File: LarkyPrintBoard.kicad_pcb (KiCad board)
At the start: 2 copper layers, 35.1 x 51.6 mm, 18 parts, among them J1 EXT1_IN, J2 EXT2_IN, J3 EXT1_OUT, J4 EXT2_OUT, J5 UART, J6 EN, J7 BOOT, U1 LM1117-3.3, U2 ESP32-WROOM, U3 CBT3257A, U4 CBT3257A

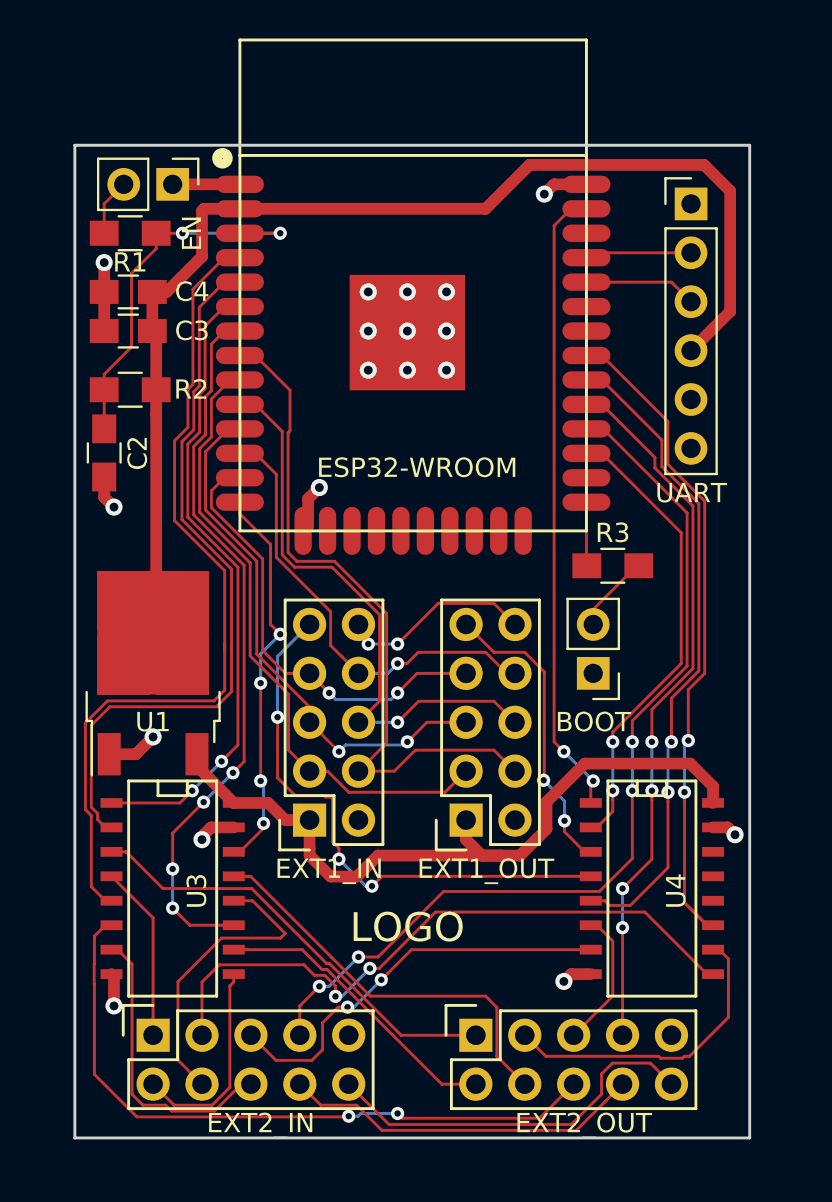
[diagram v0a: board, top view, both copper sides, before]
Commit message: Fix output pins on input only ESP32 pins. Add JTAG. Tweaks and improvements.
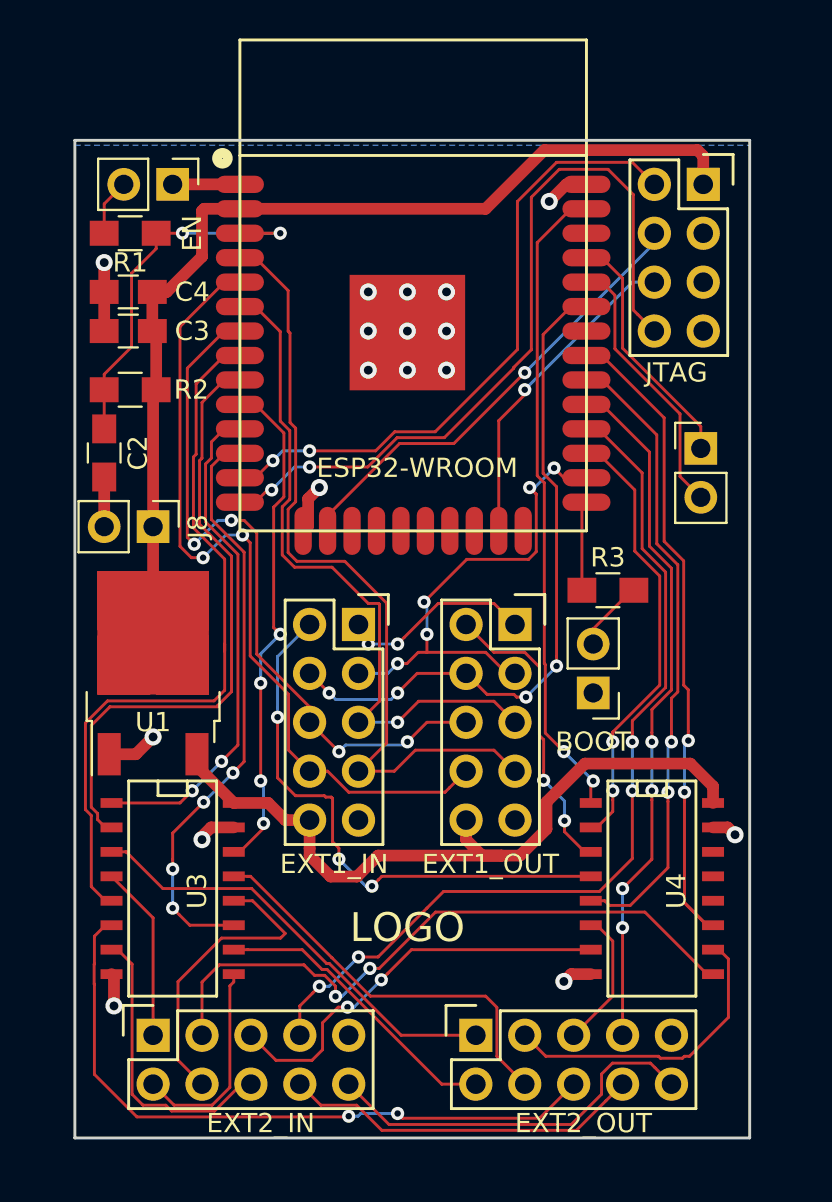
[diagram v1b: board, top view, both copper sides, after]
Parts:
- added J8: 3V3, Pin_Headers:Pin_Header_Straight_1x02_Pitch2.54mm, F.Cu at (149.4, 99.1)
- added J9: JTAG, Socket_Strips:Socket_Strip_Straight_2x04, F.Cu at (177.9, 81.3)
- J5: footprint Pin_Headers:Pin_Header_Straight_1x06_Pitch2.54mm -> Pin_Headers:Pin_Header_Straight_1x02_Pitch2.54mm
- moved J5 12.7 mm to (177.8, 95.0)
- moved J1 10.5 mm to (160.0, 104.1), turned to 270 degrees
- moved J3 10.5 mm to (168.1, 104.1), turned to 270 degrees
- moved R3 1.30 mm to (173.0, 102.4)
- moved J7 1.02 mm to (172.2, 107.7)
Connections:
- J1 pad 1: +5V -> /BEEP
- J1 pad 10: /BEEP -> +5V
- J1 pad 2: GND -> /ENC_BTN_I
- J1 pad 3: /LCD7 -> /LCD_EN
- J1 pad 4: /LCD6 -> /LCD_RS
- J1 pad 5: /LCD5 -> /LCD4
- J1 pad 6: /LCD4 -> /LCD5
- J1 pad 7: /LCD_RS -> /LCD6
- J1 pad 8: /LCD_EN -> /LCD7
- J1 pad 9: /ENC_BTN_I -> GND
- J3 pad 1: +5V -> /BEEP
- J3 pad 10: /BEEP -> +5V
- J3 pad 2: GND -> /ENC_BTN_O
- J3 pad 3: /LCD7 -> /LCD_EN
- J3 pad 4: /LCD6 -> /LCD_RS
- J3 pad 5: /LCD5 -> /LCD4
- J3 pad 6: /LCD4 -> /LCD5
- J3 pad 7: /LCD_RS -> /LCD6
- J3 pad 8: /LCD_EN -> /LCD7
- J3 pad 9: /ENC_BTN_O -> GND
- J5 pad 1: /DTR -> /ESP_TX
- J5 pad 2: /ESP_TX -> /ESP_RX
- U2 pad 10: /LCD4 -> /ESP_SD_SS
- U2 pad 11: /LCD5 -> /SD_MUX_S
- U2 pad 12: /LCD_EN -> /ESP_SPI_SCK
- U2 pad 13: /LCD_RS -> /JTAG_TMS
- U2 pad 14: /ESP_SD_SS -> /JTAG_TDI
- U2 pad 16: Net-(U2-Pad16) -> /JTAG_TCK
- U2 pad 23: Net-(U2-Pad23) -> /JTAG_TDO
- U2 pad 26: Net-(U2-Pad26) -> /LCD_EN
- U2 pad 33: Net-(U2-Pad33) -> /LCD_RS
- U2 pad 4: /ESP_SPI_MOSI -> /LCD6
- U2 pad 5: /ESP_SPI_MISO -> /LCD7
- U2 pad 6: /SD_MUX_S -> /LCD4
- U2 pad 7: /ESP_SPI_SCK -> /LCD5
- U2 pad 8: /LCD6 -> /ESP_SPI_MOSI
- U2 pad 9: /LCD7 -> /ESP_SPI_MISO
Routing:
- net /JTAG_TDI: track 0.00 -> 40.3 mm, vias 0 -> 2
- net /JTAG_TMS: track 0.00 -> 33.3 mm, vias 0 -> 2
- net /JTAG_TCK: track 0.00 -> 24.3 mm, vias 0 -> 1
- net /JTAG_TDO: track 0.00 -> 17.3 mm, vias 0 -> 1
- net /LCD_RS: track 23.3 -> 34.7 mm, vias 2 -> 4
- net /LCD5: track 28.0 -> 37.7 mm, vias 2 -> 4
- net /LCD7: track 32.9 -> 42.2 mm, vias 0 -> 2
- net +3V3: track 61.5 -> 52.6 mm
- net /ESP_RX: track 5.85 -> 14.1 mm
- net /ESP_TX: track 5.54 -> 13.2 mm
- net /ESP_SPI_SCK: track 37.6 -> 30.5 mm
- net /LCD4: track 30.6 -> 37.1 mm
- net /SD_MUX_S: track 33.3 -> 26.7 mm
- net /LCD6: track 36.1 -> 42.5 mm
- net /ESP_SD_SS: track 20.3 -> 26.3 mm
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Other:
- board size 35.1 x 51.6 mm -> 35.1 x 51.8 mm

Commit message: Alpha 1 final.
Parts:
- added D1: LED, LEDs:LED_0805_HandSoldering, F.Cu at (178.6, 107.4)
- added G***: LOGO, LarkyPrint:LOGO_17x8, F.Cu at (162.8, 120.7)
- added R4: 560, Resistors_SMD:R_0805_HandSoldering, F.Cu at (178.6, 102.1)
- added REF**: MountingHole_3mm, Mounting_Holes:MountingHole_3mm, F.Cu at (146.0, 78.0)
- added REF**: MountingHole_3mm, Mounting_Holes:MountingHole_3mm, F.Cu at (180.0, 78.0)
- added REF**: MountingHole_3mm, Mounting_Holes:MountingHole_3mm, F.Cu at (180.0, 130.0)
- added REF**: MountingHole_3mm, Mounting_Holes:MountingHole_3mm, F.Cu at (146.0, 130.0)
- J6: value EN -> RST
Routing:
- net +3V3: track 52.6 -> 73.4 mm
- net Net-(D1-Pad2): track 0.00 -> 2.63 mm
- net GND: track 23.8 -> 25.8 mm, vias 17 -> 18
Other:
- board size 35.1 x 51.8 mm -> 38 x 56 mm
- board text added: "Lark R1-A1 - 09.07.2017 Copyright Greg Lincoln CC BY-NC-SA"
- board text removed: "LOGO"
- board text removed: "LarkyPrint v0r1 - MM/DD/YYYY Some rights reserved."

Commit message: Tons of changes and fixes. R1A2
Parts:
- removed J9: JTAG, Socket_Strips:Socket_Strip_Straight_2x04
- removed the REF** at (146.0, 78.0)
- removed the REF** at (180.0, 78.0)
- removed the REF** at (180.0, 130.0)
- removed the REF** at (146.0, 130.0)
- removed the REF*** at (163.1, 96.5)
- added G***: LOGO, LarkyPrint:LOGO, B.Cu at (162.6, 80.8)
- added R10: 10K, Resistors_SMD:R_0805_HandSoldering, F.Cu at (148.8, 101.9)
- added R11: 680, Resistors_SMD:R_0805_HandSoldering, F.Cu at (173.0, 104.1)
- added R5: 10K, Resistors_SMD:R_0805_HandSoldering, F.Cu at (157.2, 119.7)
- added R6: 10K, Resistors_SMD:R_0805_HandSoldering, F.Cu at (168.7, 119.7)
- added R7: 10K, Resistors_SMD:R_0805_HandSoldering, F.Cu at (178.6, 112.5)
- added R8: 10K, Resistors_SMD:R_0805_HandSoldering, F.Cu at (147.3, 113.7)
- added R9: 10K, Resistors_SMD:R_0805_HandSoldering, F.Cu at (148.8, 103.6)
- added REF**: MountingHole_2.2mm_M2, Mounting_Holes:MountingHole_2.2mm_M2, F.Cu at (146.0, 130.0)
- added REF**: MountingHole_2.2mm_M2, Mounting_Holes:MountingHole_2.2mm_M2, F.Cu at (180.0, 130.0)
- added REF**: MountingHole_2.2mm_M2, Mounting_Holes:MountingHole_2.2mm_M2, F.Cu at (180.0, 78.0)
- added REF***: OSHW-Logo_5.7x6mm_SilkScreen, Symbols:OSHW-Logo_5.7x6mm_SilkScreen, B.Cu at (162.8, 97.2)
- C3: footprint Capacitors_SMD:C_0805_HandSoldering -> Capacitors_SMD:C_1206_HandSoldering
- J1: value EXT1_IN -> EXT1 Printer; footprint Socket_Strips:Socket_Strip_Straight_2x05 -> Pin_Headers:Pin_Header_Straight_2x05_Pitch2.54mm
- J2: value EXT2_IN -> EXT2 LCD; footprint Socket_Strips:Socket_Strip_Straight_2x05 -> Pin_Headers:Pin_Header_Straight_2x05_Pitch2.54mm
- J3: value EXT1_OUT -> EXT1 LCD; footprint Socket_Strips:Socket_Strip_Straight_2x05 -> Pin_Headers:Pin_Header_Straight_2x05_Pitch2.54mm
- J4: value EXT2_OUT -> EXT2 Printer; footprint Socket_Strips:Socket_Strip_Straight_2x05 -> Pin_Headers:Pin_Header_Straight_2x05_Pitch2.54mm
- J5: footprint Pin_Headers:Pin_Header_Straight_1x02_Pitch2.54mm -> Pin_Headers:Pin_Header_Straight_1x05_Pitch2.54mm
- J6: value RST -> EN
- R1, R3: value 470 -> 680
- R2: value 12K -> 10K
- R4: value 560 -> 680
- moved D1 41.3 mm to (148.8, 78.7), turned to 180 degrees
- moved R4 36.7 mm to (148.8, 80.5), turned to 0 degrees
- moved G*** 24.7 mm to (178.6, 101.6), turned to 90 degrees
- moved J6 13.0 mm to (150.1, 94.2)
- moved J1 11.4 mm to (167.8, 112.5)
- moved C3 6.40 mm to (148.8, 82.5)
- moved C2 5.45 mm to (148.8, 90.2), turned to 180 degrees
- moved R2 5.38 mm to (148.8, 86.6), turned to 0 degrees
- moved R1 4.62 mm to (148.8, 88.4)
- moved U1 2.67 mm to (150.2, 109.2), turned to 180 degrees
- moved J2 2.54 mm to (149.4, 128.0), turned to 90 degrees
- moved J4 2.54 mm to (166.1, 128.0), turned to 90 degrees
- moved J5 2.54 mm to (177.8, 92.5), turned to 180 degrees
- moved C4 2.18 mm to (148.8, 84.8), turned to 180 degrees
- moved J8 1.93 mm to (147.6, 98.3), turned to 90 degrees
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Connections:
- J5 pad 1: /ESP_TX -> /ESP_RX
- J5 pad 2: /ESP_RX -> /ESP_TX
- U2 pad 10: /ESP_SD_SS -> Net-(U2-Pad10)
- U2 pad 11: /SD_MUX_S -> Net-(U2-Pad11)
- U2 pad 12: /ESP_SPI_SCK -> Net-(U2-Pad12)
- U2 pad 13: /JTAG_TMS -> /ESP_SPI_SCK
- U2 pad 14: /JTAG_TDI -> Net-(U2-Pad14)
- U2 pad 16: /JTAG_TCK -> /LCD_RS
- U2 pad 23: /JTAG_TDO -> /ESP_SPI_MOSI
- U2 pad 24: Net-(U2-Pad24) -> /ESP_SPI_MISO
- U2 pad 33: /LCD_RS -> /ENC_MUX_S
- U2 pad 36: Net-(U2-Pad36) -> /ESP_SD_SS
- U2 pad 37: /ENC_MUX_S -> /SD_MUX_S
- U2 pad 4: /LCD6 -> /LCD5
- U2 pad 5: /LCD7 -> /LCD4
- U2 pad 6: /LCD4 -> /LCD6
- U2 pad 7: /LCD5 -> /LCD7
- U2 pad 8: /ESP_SPI_MOSI -> Net-(U2-Pad8)
- U2 pad 9: /ESP_SPI_MISO -> Net-(U2-Pad9)
- U4 pad 10: /ENC_2_O -> /ENC_2_I
- U4 pad 6: /ENC_1_O -> /ENC_1_I
- U4 pad 7: /ENC_1_I -> /ENC_1_O
- U4 pad 9: /ENC_2_I -> /ENC_2_O
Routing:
- net /JTAG_TDI: track 40.3 -> 0.00 mm, vias 2 -> 0
- net /JTAG_TMS: track 33.3 -> 0.00 mm, vias 2 -> 0
- net +3V3: track 73.4 -> 40.4 mm
- net /ESP_SD_SS: track 26.3 -> 53.1 mm, vias 4 -> 2
- net /SD_MUX_S: track 26.7 -> 51.7 mm
- net /JTAG_TCK: track 24.3 -> 0.00 mm, vias 1 -> 0
- net /JTAG_TDO: track 17.3 -> 0.00 mm, vias 1 -> 0
- net /ENC_BTN_I: track 29.1 -> 12.3 mm, vias 3 -> 1
- net /ENC_1_I: track 21.4 -> 36.8 mm, vias 2 -> 0
- net /SD_MISO_I: track 9.15 -> 23.1 mm
- net /ESP_SPI_MISO: track 32.7 -> 45.6 mm, vias 0 -> 4
- net /SD_SS_I: track 15.8 -> 3.71 mm
- net /LCD6: track 42.5 -> 30.7 mm, vias 0 -> 1
- net /EN: track 19.8 -> 8.42 mm, vias 2 -> 0
- net /ENC_2_O: track 16.3 -> 26.0 mm, vias 0 -> 1
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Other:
- rule pad_to_mask_clearance: 0.2 -> 0.0762
- board text added: "Lark R1-A2 - 09.23.2017 Copyright Greg Lincoln CC BY-NC-SA"
- board text removed: "Lark R1-A1 - 09.07.2017 Copyright Greg Lincoln CC BY-NC-SA"

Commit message: Minor tweaks.
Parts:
- J6: footprint Pin_Headers:Pin_Header_Straight_1x02_Pitch2.54mm -> LarkyPrint:KXT131LHS
- moved J6 1.27 mm to (148.8, 94.2), turned to 0 degrees
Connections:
- J6 pad 1: GND -> Net-(J6-Pad1)
- J6 pad 2: Net-(J6-Pad2) -> GND
- R1 pad 2: Net-(J6-Pad2) -> Net-(J6-Pad1)
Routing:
- net Net-(J6-Pad2): track 6.75 -> 0.00 mm
- net Net-(J6-Pad1): track 0.00 -> 6.61 mm
- net GND: track 27.4 -> 31.7 mm
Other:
- board text added: "+"
